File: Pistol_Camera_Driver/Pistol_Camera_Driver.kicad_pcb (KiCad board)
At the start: 2 copper layers, 45 parts, among them J1 Screw_Terminal_01x02, J2 Conn_01x08, J3 Screw_Terminal_01x02, J4 Screw_Terminal_01x02, J5 Conn_01x04_Female, J6 Joystick, J7 Screw_Terminal_01x02, J8 Screw_Terminal_01x03, Q1 IRLML6402, U1 LM7805_TO220, U2 LM317_TO-263, U3 Raspberri_Pi_Pico, U4 DRV8834PWP, U5 DRV8834PWP, U6 LDD-700L, U7 LDD-700L

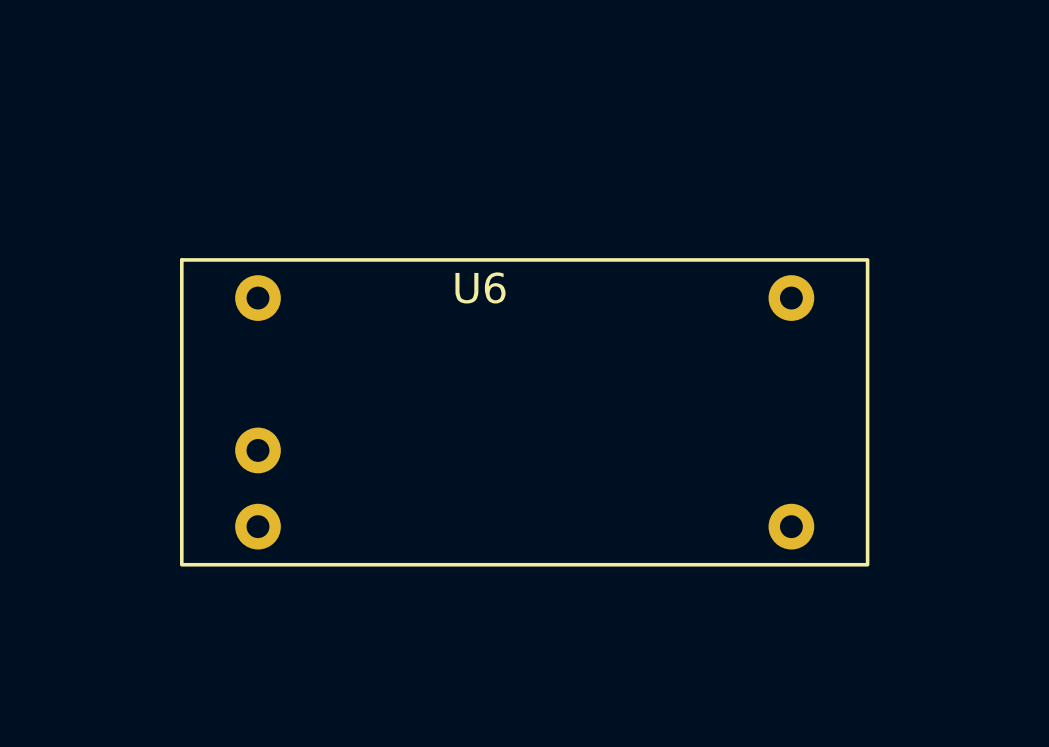
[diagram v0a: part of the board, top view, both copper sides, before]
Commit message: v0.72 level translaors have been added
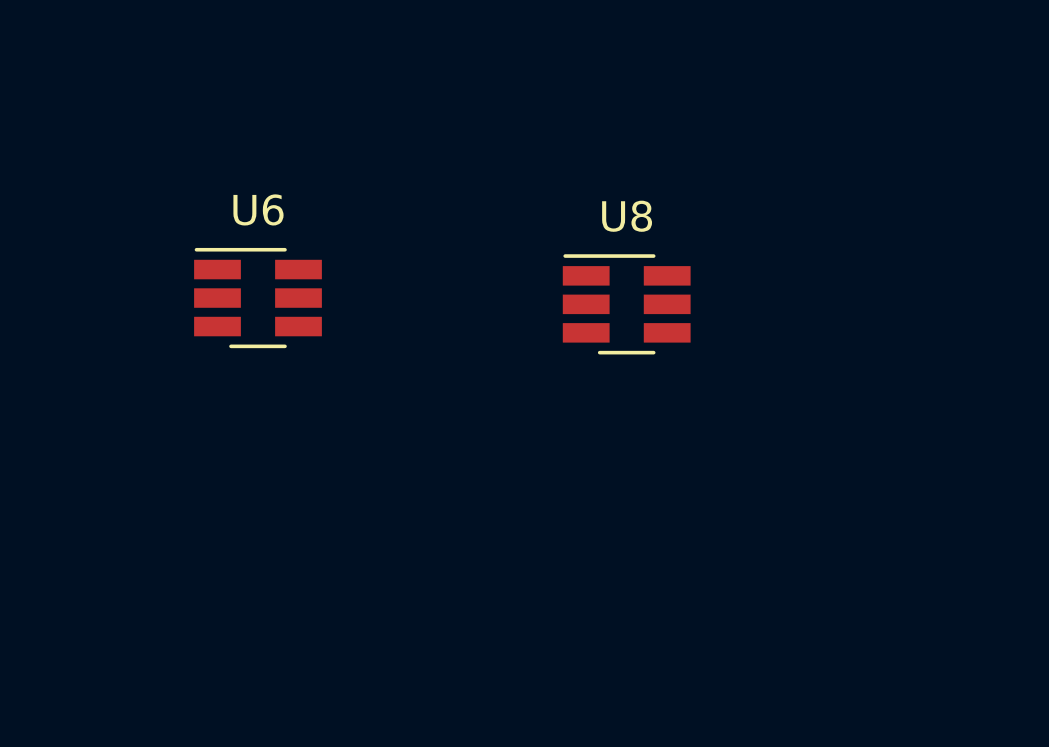
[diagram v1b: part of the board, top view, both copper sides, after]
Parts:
- added U8: RS0101YH6, Package_TO_SOT_SMD:SOT-23-6_Handsoldering, F.Cu at (112.8, 85.6)
- C1, C9: value C_Polarized -> 10uF
- C10, C3, C5: value C -> 0.1
- C11, C7: value C -> 0.01
- C12, C8: value C -> 2.2
- C2: value C -> 0.33
- C4, C6: value C -> 1
- J2: value Conn_01x08 -> Objective
- J5: value Conn_01x04_Female -> SONAR
- R1, R9: value R -> 47k
- R7: value R -> 10k
- U6: value LDD-700L -> RS0101YH6; footprint Shield_Emergent:LDD-700L -> Package_TO_SOT_SMD:SOT-23-6_Handsoldering
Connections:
- C1 pad 1: +3V3 -> +3.3VP
- C10 pad 1: +3V3 -> +3.3VP
- C11 pad 2: +3V3 -> +3.3VP
- C5 pad 2: +3V3 -> +3.3VP
- C6 pad 1: +3V3 -> +3.3VP
- C7 pad 2: +3V3 -> +3.3VP
- C9 pad 1: +3V3 -> +3.3VP
- R13 pad 1: +3V3 -> +3.3VP
- R15 pad 1: PWM_UV -> Net-(R15-Pad1)
- R15 pad 2: +5V -> GND
- R3 pad 1: +3V3 -> +3.3VP
- R7 pad 1: +3V3 -> +3.3VP
- R9 pad 1: +3V3 -> +3.3VP
- U2 pad 2: +3V3 -> +3.3VP
- U3 pad 37: unconnected-(U3-Pad37) -> +3V3
- U4 pad 18: +3V3 -> +3.3VP
- U4 pad 19: +3V3 -> +3.3VP
- U5 pad 18: +3V3 -> +3.3VP
- U5 pad 19: +3V3 -> +3.3VP
- U6 pad 1: +12V -> +3V3
- U6 pad 2: Net-(Q1-Pad3) -> GND
- U6 pad 3: GND -> PWM_UV
- U6 pad 4: Net-(D2-Pad1) -> Net-(R15-Pad1)
- U6 pad 5: Net-(D1-Pad2) -> +3V3
- U7 pad 2: PWM_WHITE -> Net-(R15-Pad1)
- U7 pad 4: Net-(D4-Pad1) -> Net-(D2-Pad1)
- U7 pad 5: Net-(D3-Pad2) -> Net-(D1-Pad2)

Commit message: v0.8 first decomposition is completed
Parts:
- removed Q1: IRLML6402, Package_TO_SOT_SMD:SOT-23
- added J9: Screw_Terminal_01x02, Connector_PinSocket_2.54mm:PinSocket_1x02_P2.54mm_Vertical, F.Cu at (164.7, 44.5)
- added U10: RS0101YH6, Package_TO_SOT_SMD:SOT-23-6_Handsoldering, F.Cu at (133.8, 45.6)
- added U11: LDD-700L, Shield_Emergent:LDD-700L, F.Cu at (139.8, 41.8)
- added U9: LDD-700L, Shield_Emergent:LDD-700L, F.Cu at (139.8, 30.7)
- J3: value Screw_Terminal_01x02 -> 12V power
- J4: value Screw_Terminal_01x02 -> FAN
- J8: value Screw_Terminal_01x03 -> Screw_Terminal_01x04; footprint Connector_PinSocket_2.54mm:PinSocket_1x03_P2.54mm_Vertical -> Connector_PinHeader_2.54mm:PinHeader_1x04_P2.54mm_Vertical
- moved R13 94.9 mm to (189.8, 42.9), turned to -90 degrees
- moved R14 88.6 mm to (176.3, 44.7)
- moved R8 88.2 mm to (177.5, 55.1)
- moved C2 88.0 mm to (64.3, 56.5), turned to 90 degrees
- moved C4 85.4 mm to (71.7, 47.7), turned to 180 degrees
- moved C6 84.8 mm to (62.9, 39.1), turned to -90 degrees
- moved R5 81.7 mm to (177.6, 53.3)
- moved U4 79.2 mm to (183.6, 53.6), turned to -90 degrees
- moved R10 77.2 mm to (177.2, 37.9)
- moved C9 70.2 mm to (195.2, 42.9), turned to 90 degrees
- moved C3 67.6 mm to (73.7, 57.5), turned to -90 degrees
- moved U7 66.2 mm to (139.8, 53.2)
- moved R7 65.4 mm to (190.2, 54.8), turned to -90 degrees
- moved J7 63.6 mm to (164.6, 55.2)
- moved Je1 62.0 mm to (164.8, 33.5)
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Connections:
- J6 pad 3: VarX -> VarY
- J6 pad 4: VarY -> VarX
- J8 pad 3: GND -> PWM_RED
- U3 pad 6: unconnected-(U3-Pad6) -> PWM_RED
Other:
- board outline added: 140.7 x 46.6 mm

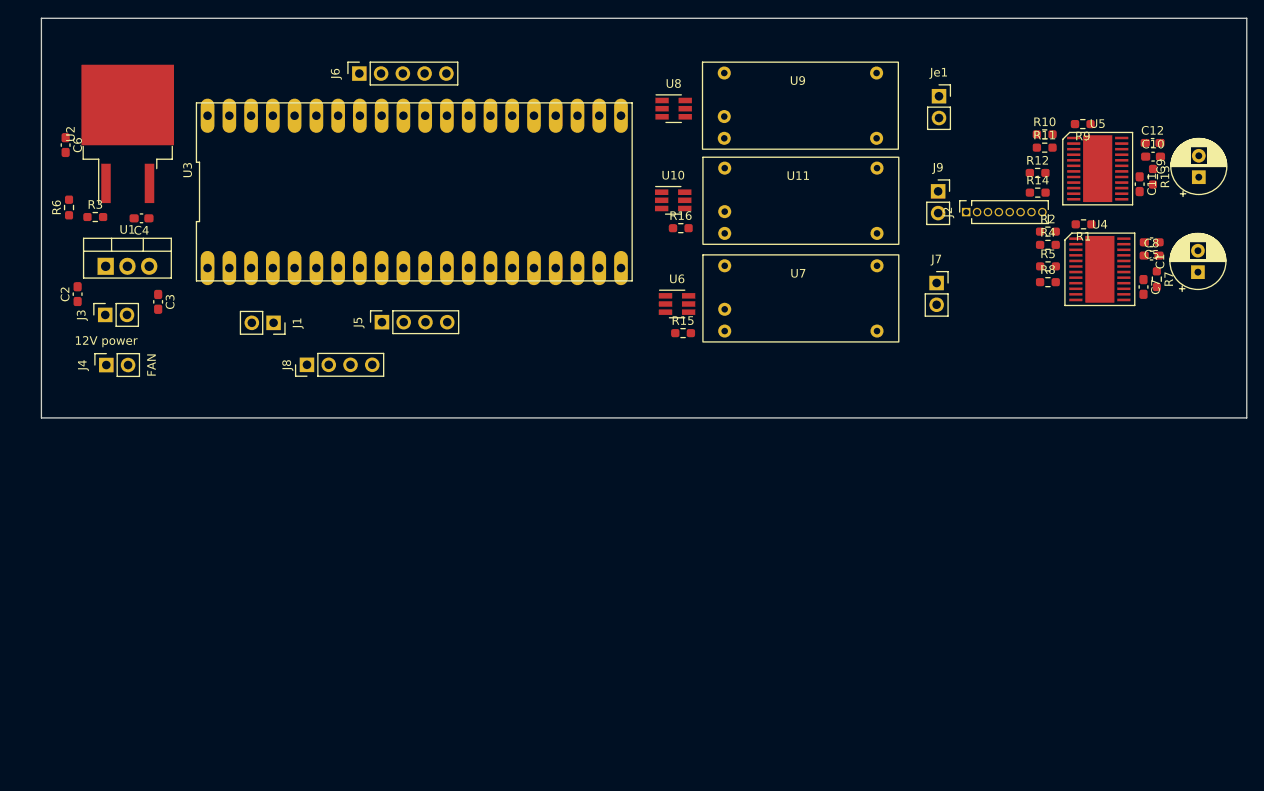
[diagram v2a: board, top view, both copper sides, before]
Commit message: v0.9 PCB size has been decreased
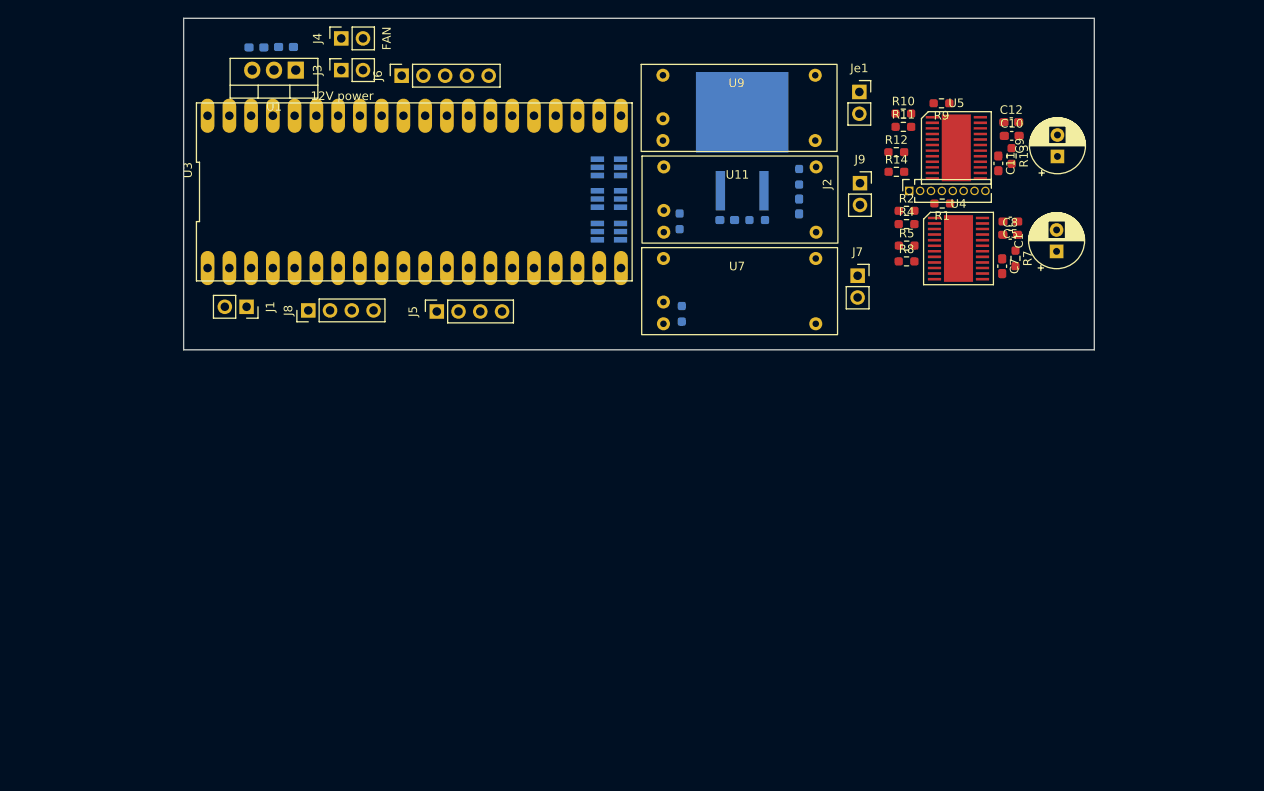
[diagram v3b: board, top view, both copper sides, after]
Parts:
- C2, C3, C4, C6, R15, R16, R3, R6, U10, U2, U6, U8: moved to B.Cu
- moved C6 85.9 mm to (148.5, 46.3)
- moved R3 82.3 mm to (148.5, 42.9), turned to -90 degrees
- moved R6 80.3 mm to (143.6, 47.9), turned to 180 degrees
- moved U2 71.7 mm to (141.8, 38.7)
- moved C4 68.4 mm to (140.1, 47.9), turned to 0 degrees
- moved J4 47.0 mm to (95.0, 26.7)
- moved J3 39.7 mm to (95.0, 30.4)
- moved C2 37.7 mm to (88.6, 27.7), turned to 180 degrees
- moved U1 31.9 mm to (89.7, 30.4), turned to 180 degrees
- moved C3 31.8 mm to (85.2, 27.8), turned to 0 degrees
- moved C1 16.7 mm to (178.6, 51.6)
- moved C10 16.7 mm to (173.3, 38.1)
- moved C11 16.7 mm to (171.8, 41.3)
- moved C12 16.7 mm to (173.3, 36.5)
- moved C5 16.7 mm to (173.2, 48.1)
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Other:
- board size 140.7 x 46.6 mm -> 106.3 x 38.7 mm

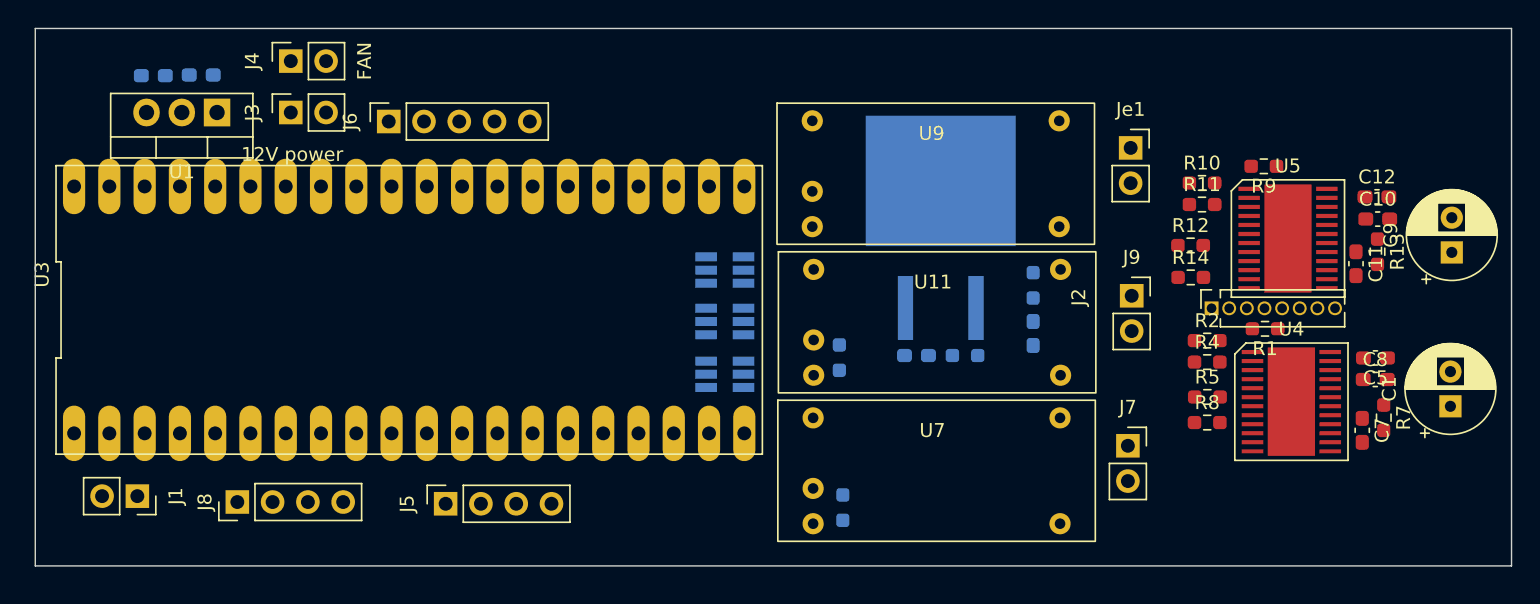
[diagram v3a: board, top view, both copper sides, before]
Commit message: v1.0 decomposition has been completed. Partial routing
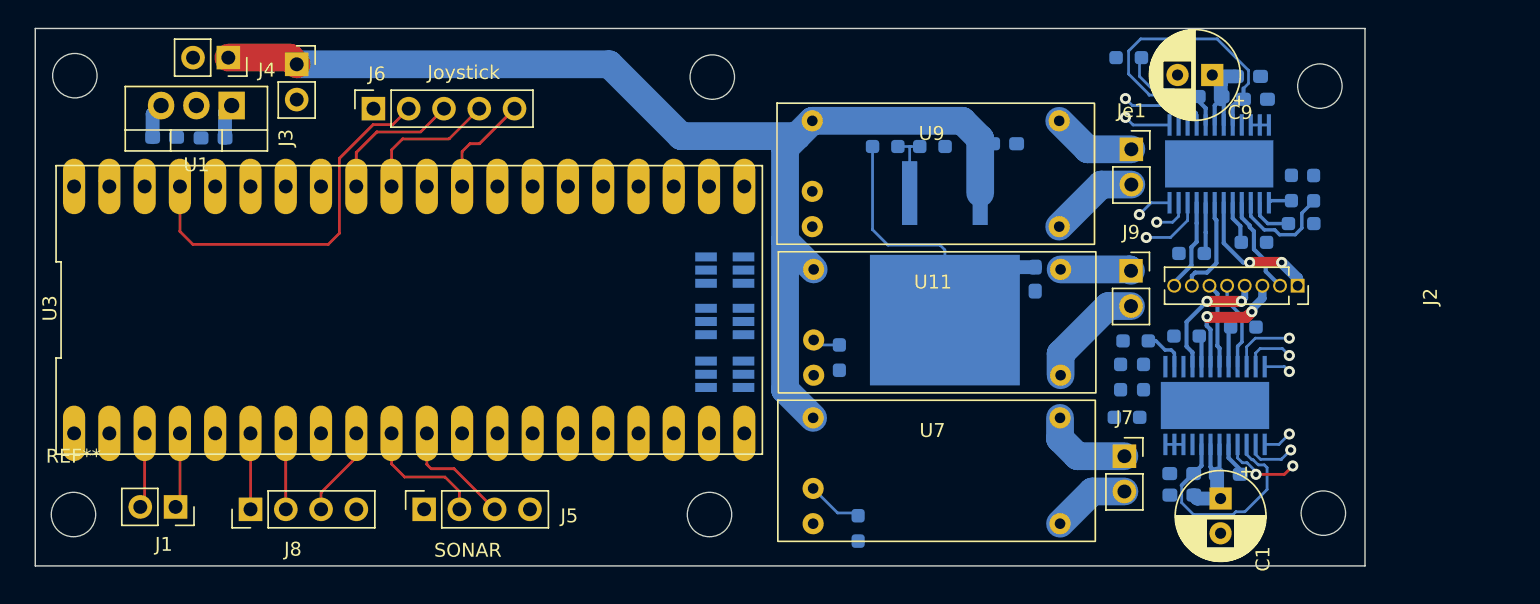
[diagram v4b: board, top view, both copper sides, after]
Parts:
- added REF**: MountingHole_3.2mm_M3, MountingHole:MountingHole_3.2mm_M3, F.Cu at (125.2, 59.4)
- added REF**: MountingHole_3.2mm_M3, MountingHole:MountingHole_3.2mm_M3, F.Cu at (125.4, 27.9)
- added REF**: MountingHole_3.2mm_M3, MountingHole:MountingHole_3.2mm_M3, F.Cu at (79.5, 27.8)
- added REF**: MountingHole_3.2mm_M3, MountingHole:MountingHole_3.2mm_M3, F.Cu at (169.4, 59.2)
- added REF**: MountingHole_3.2mm_M3, MountingHole:MountingHole_3.2mm_M3, F.Cu at (79.4, 59.4)
- added REF**: MountingHole_3.2mm_M3, MountingHole:MountingHole_3.2mm_M3, F.Cu at (169.2, 28.5)
- C10, C11, C12, C5, C7, C8, R1, R10, R11, R12, R13, R14, R2, R4, R5, R7, R8, R9, U4, U5: moved to B.Cu
- J3: value 12V power -> Screw_Terminal_01x02
- J4: value FAN -> Screw_Terminal_01x02
- moved R13 22.7 mm to (155.4, 26.4), turned to 0 degrees
- moved C9 21.5 mm to (161.4, 27.7), turned to 180 degrees
- moved R7 18.5 mm to (155.3, 52.4), turned to 0 degrees
- moved C1 17.8 mm to (162.0, 58.2), turned to -90 degrees
- moved C5 17.1 mm to (159.2, 58.0), turned to 0 degrees
- moved C4 16.5 mm to (146.4, 32.6)
- moved C11 16.0 mm to (161.2, 29.2), turned to 0 degrees
- moved C8 15.5 mm to (159.2, 56.4), turned to 180 degrees
- moved R6 15.2 mm to (141.2, 32.9), turned to 0 degrees
- moved R3 14.6 mm to (137.8, 32.9), turned to 0 degrees
- moved C10 13.9 mm to (164.0, 27.8)
- moved C12 11.2 mm to (164.5, 29.4)
- moved C7 10.2 mm to (162.6, 56.5), turned to 180 degrees
- moved R1 9.41 mm to (156.4, 49.5), turned to 90 degrees
- moved R11 8.12 mm to (168.7, 35.9), turned to -90 degrees
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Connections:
- C3 pad 1: +5V -> Net-(C3-Pad1)
- C4 pad 1: +5V -> +12V
- J8 pad 1: PWM_UV -> PWM_RED
- J8 pad 2: PWM_WHITE -> PWM_UV
- J8 pad 3: PWM_RED -> PWM_WHITE
- R13 pad 1: +3.3VP -> +3V3
- R13 pad 2: Net-(R13-Pad2) -> nFLT2
- R7 pad 1: +3.3VP -> +3V3
- R7 pad 2: Net-(R7-Pad2) -> nFLT1
- U1 pad 3: +5V -> Net-(C3-Pad1)
- U2 pad 3: +5V -> +12V
- U3 pad 12: unconnected-(U3-Pad12) -> MOTORS_nSLEEP
- U3 pad 14: MOTORS_nSLEEP -> nFLT1
- U3 pad 27: unconnected-(U3-Pad27) -> nFLT2
- U4 pad 16: Net-(R7-Pad2) -> nFLT1
- U5 pad 16: Net-(R13-Pad2) -> nFLT2
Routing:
- net +12V: track 0.00 -> 88.4 mm
- net +3.3VP: track 0.00 -> 47.0 mm
- net +3V3: track 0.00 -> 27.3 mm
- net Net-(C12-Pad1): track 0.00 -> 22.5 mm
- net Net-(C8-Pad1): track 0.00 -> 17.0 mm
- net VarX: track 0.00 -> 10.2 mm
- net AOUT2_1: track 0.00 -> 10.1 mm, vias 0 -> 2
- net VarY: track 0.00 -> 10.1 mm
- net AOUT2_2: track 0.00 -> 9.81 mm, vias 0 -> 2
- net AOUT1_1: track 0.00 -> 9.22 mm, vias 0 -> 2
- net TRIG: track 0.00 -> 9.19 mm
- net ECHO: track 0.00 -> 8.46 mm
- net BOUT1_2: track 0.00 -> 8.15 mm
- net Net-(D6-Pad1): track 0.00 -> 8.04 mm
- net Net-(R11-Pad2): track 0.00 -> 7.71 mm
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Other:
- board size 106.3 x 38.7 mm -> 95.8 x 38.7 mm

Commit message: v1.1 The first iteration of routing
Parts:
- moved U8 2.88 mm to (123.5, 40.9)
- moved U10 2.84 mm to (123.5, 44.8)
- moved U6 2.83 mm to (123.5, 48.6)
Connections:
- C3 pad 1: Net-(C3-Pad1) -> +5V
- U1 pad 3: Net-(C3-Pad1) -> +5V
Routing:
- net +5V: track 0.54 -> 72.8 mm, vias 0 -> 3
- net nEN1: track 4.76 -> 74.2 mm
- net +3V3: track 27.3 -> 93.9 mm, vias 0 -> 3
- net PWM_WHITE: track 6.52 -> 59.7 mm
- net STEP1: track 3.74 -> 56.2 mm
- net DIR1: track 1.92 -> 50.8 mm
- net nFLT2: track 7.48 -> 55.2 mm, vias 0 -> 1
- net M0_1: track 2.09 -> 49.6 mm
- net nEN2: track 4.76 -> 51.5 mm
- net M1_1: track 3.74 -> 49.6 mm
- net STEP2: track 2.73 -> 45.9 mm
- net DIR2: track 2.53 -> 42.5 mm
- net PWM_UV: track 5.47 -> 39.6 mm
- net M0_2: track 3.40 -> 37.2 mm
- net PWM_RED: track 5.47 -> 39.1 mm
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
